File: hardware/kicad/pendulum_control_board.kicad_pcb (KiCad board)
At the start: 2 copper layers, 103.3 x 112.3 mm, 267 parts, among them IC1 STM32F411CEU6, IC2 LM358D, J1 DX07S024JJ2, Q1 BSS138, Q2 BSS138, Q3 BSS138, Q4 BSS138, Q5 2N7002, Q6 2N7002, Q7 2N7002, U1 FT231XS, U2 V_REG_317SMD, U3 V_REG_317SMD, U5 LTC6102DD, X1 5566-8, X2 5566-8, Y2 32.768kHz

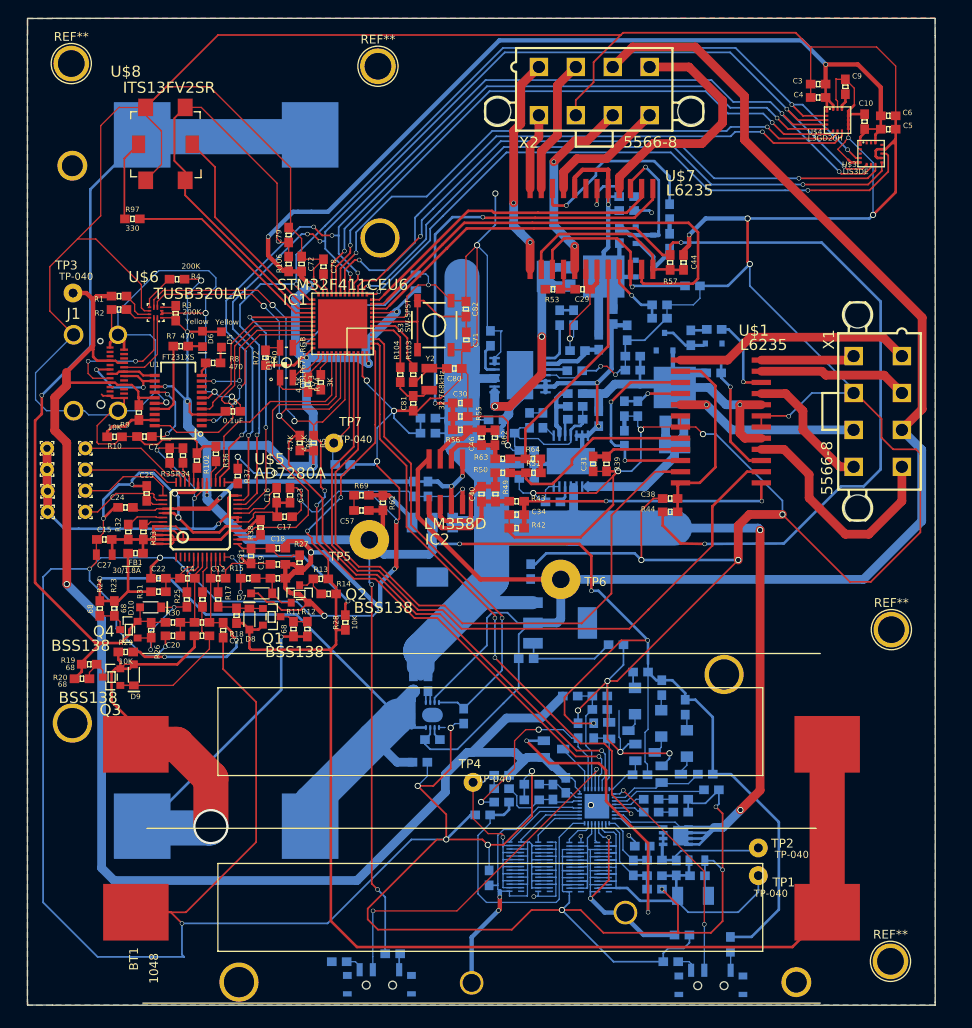
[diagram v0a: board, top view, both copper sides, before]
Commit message: updated PCB and created schematic pdf
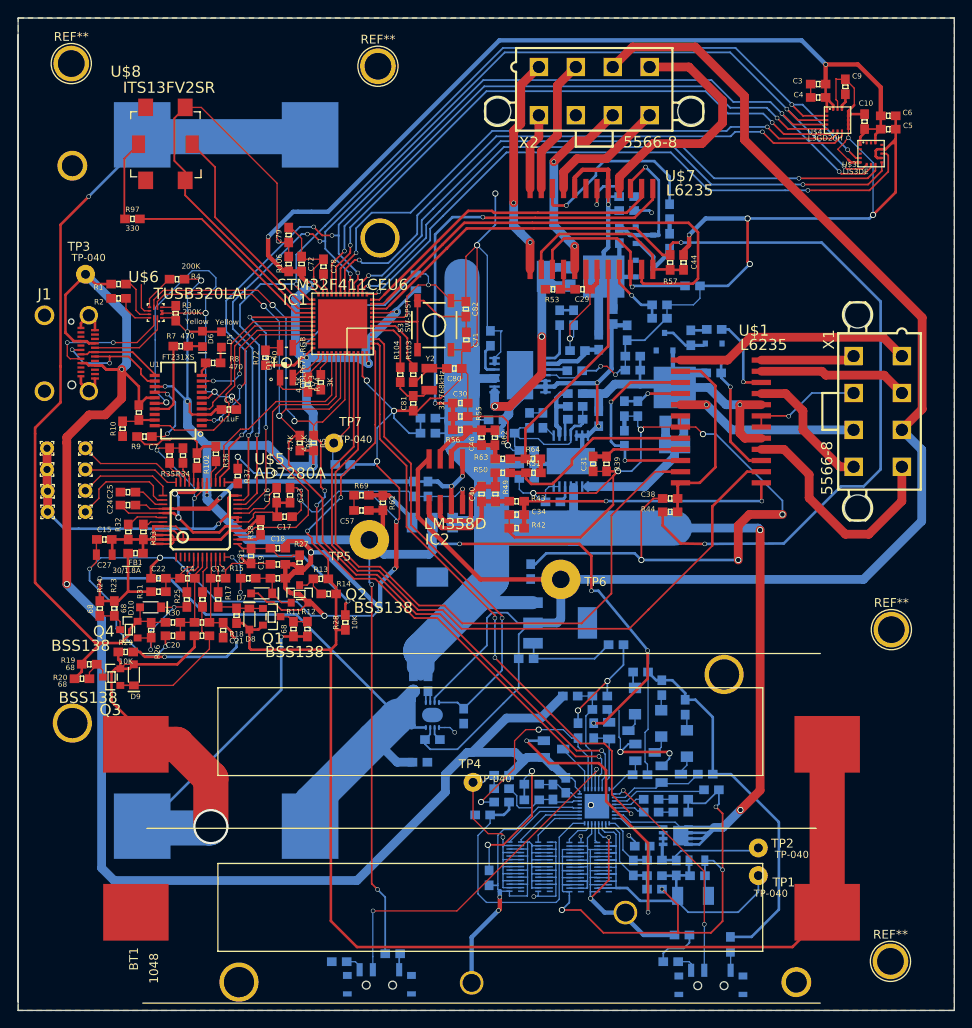
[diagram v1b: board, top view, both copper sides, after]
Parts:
- moved J1 3.99 mm to (53.6, 84.6)
- moved TP3 2.56 mm to (55.3, 79.2)
- moved C25 2.14 mm to (60.1, 104.0), turned to 180 degrees
- moved R1 1.37 mm to (59.0, 80.3)
- moved R10 1.29 mm to (59.5, 96.8), turned to 90 degrees
- moved R2 1.27 mm to (59.0, 81.9)
- moved C8 0.50 mm to (71.6, 94.6)
- moved C24 0.39 mm to (60.1, 105.5)
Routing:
- net GND: track 1439.6 -> 869.8 mm, vias 64 -> 59
- net /3P3V: track 422.8 -> 415.6 mm
- net /DP: track 5.36 -> 9.68 mm
- net /V_BUS: track 194.3 -> 190.8 mm, vias 1 -> 2
- net /N$10: track 6.55 -> 3.72 mm
- net /DM: track 12.3 -> 15.0 mm
- net /T_CELL1: track 10.3 -> 12.4 mm
- net /CREF: track 1.69 -> 3.71 mm
- net /UART_RXD: track 29.4 -> 27.6 mm
- net /N$6: track 3.91 -> 5.49 mm
- net /N$1: track 3.01 -> 4.31 mm
- net /DEN_GYRO: track 69.9 -> 68.8 mm
- net /CC2: track 15.8 -> 14.8 mm
- net /CC1: track 8.58 -> 9.30 mm
- net /ALERT_BATT: track 24.6 -> 23.9 mm
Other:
- board size 103.3 x 112.3 mm -> 106.5 x 112.9 mm

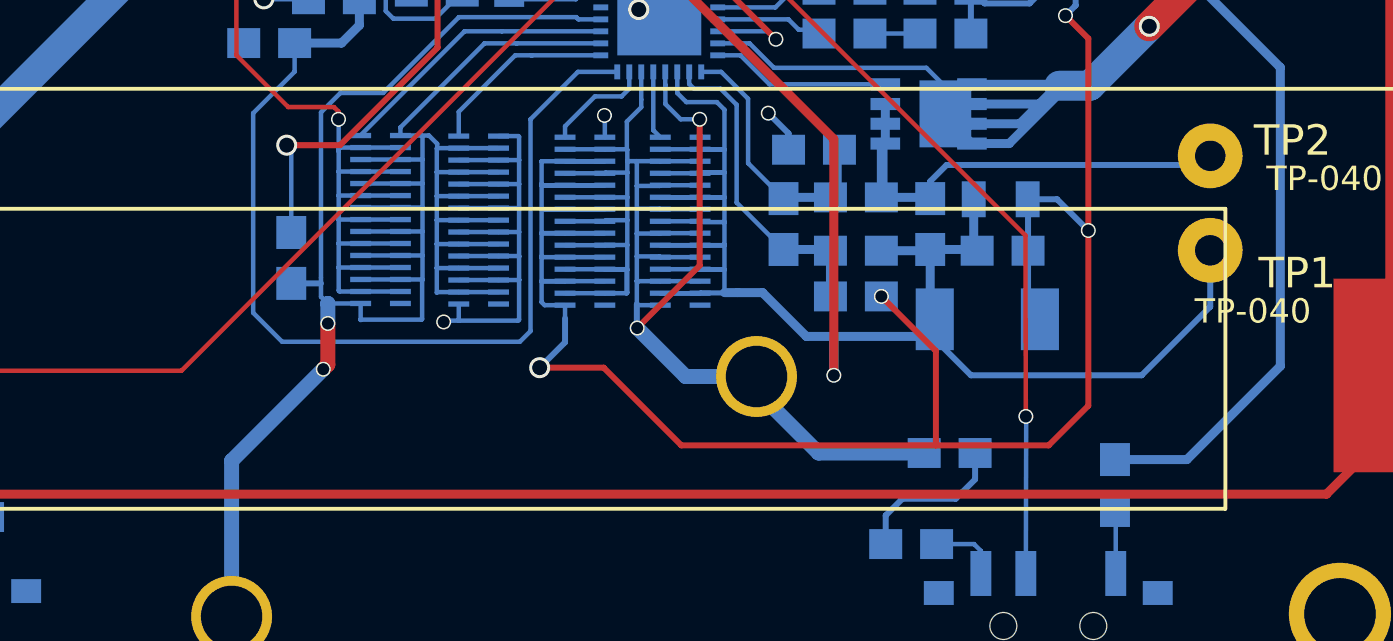
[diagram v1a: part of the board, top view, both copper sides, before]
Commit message: added schottkys to charging circuit
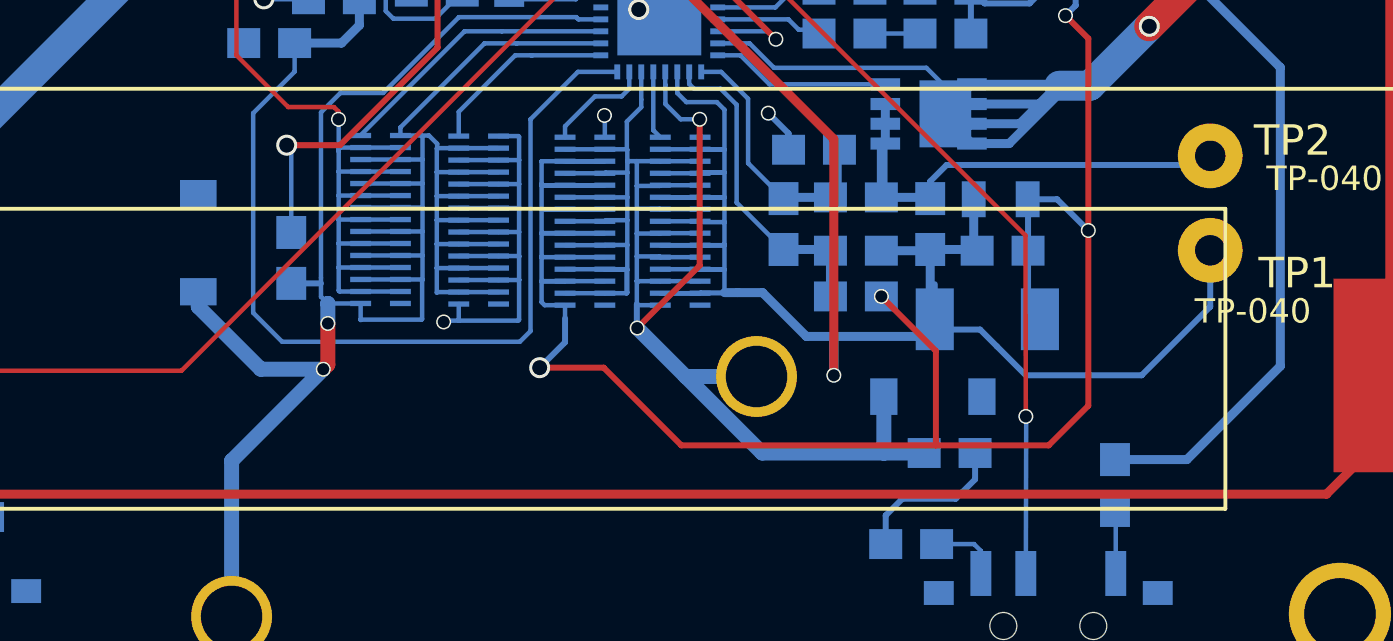
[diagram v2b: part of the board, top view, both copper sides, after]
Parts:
- added D1: MBR0520, Diodes_SMD:SOD-123, B.Cu at (98.1, 147.4)
- added D17: MBR0520, Diodes_SMD:SOD-123, B.Cu at (122.6, 152.5)
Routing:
- net /N$62: track 81.0 -> 86.5 mm
- net /N$65: track 65.6 -> 70.1 mm
- net /VSYS+: track 93.7 -> 94.5 mm
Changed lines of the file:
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@@
 (kicad_pcb (version 4) (host pcbnew 4.0.2+dfsg1-stable)
   (general
-    (links 731)
+    (links 735)
     (no_connects 0)
-    (area 44.840853 50.026099 152.005501 163.209581)
+    (area 47.536899 49.987999 154.177201 163.016401)
     (thickness 1.6)
     (drawings 6)
-    (tracks 2909)
+    (tracks 2920)
     (zones 0)
-    (modules 267)
+    (modules 269)
     (nets 195)
   )
@@
   )
   (setup
-    (last_trace_width 0.2)
+    (last_trace_width 0.5)
     (user_trace_width 0.15)
     (user_trace_width 0.2)
@@
     (pad 1 thru_hole circle (at 0 0) (size 4.064 4.064) (drill 3.048) (layers *.Cu *.Mask F.SilkS))
   )
+  (module Diodes_SMD:SOD-123 (layer B.Cu)
+    (at 98.0948 147.3708 90)
+    (descr SOD-123)
+    (tags SOD-123)
+    (attr smd)
+    (fp_text reference D1 (at 2.8956 -0.254 180) (layer B.SilkS)
+      (effects (font (size 1 1) (thickness 0.15)) (justify mirror))
+    )
+    (fp_text value MBR0520 (at 0.6604 -1.8796 90) (layer B.SilkS)
+      (effects (font (size 1 1) (thickness 0.15)) (justify mirror))
+    )
+    (fp_line (start 0.3175 0) (end 0.6985 0) (layer B.SilkS) (width 0.15))
+    (fp_line (start -0.6985 0) (end -0.3175 0) (layer B.SilkS) (width 0.15))
+    (fp_line (start -0.3175 0) (end 0.3175 0.381) (layer B.SilkS) (width 0.15))
+    (fp_line (start 0.3175 0.381) (end 0.3175 -0.381) (layer B.SilkS) (width 0.15))
+    (fp_line (start 0.3175 -0.381) (end -0.3175 0) (layer B.SilkS) (width 0.15))
+    (fp_line (start -0.3175 0.508) (end -0.3175 -0.508) (layer B.SilkS) (width 0.15))
+    (fp_line (start -2.25 1.05) (end 2.25 1.05) (layer B.CrtYd) (width 0.05))
+    (fp_line (start 2.25 1.05) (end 2.25 -1.05) (layer B.CrtYd) (width 0.05))
+    (fp_line (start 2.25 -1.05) (end -2.25 -1.05) (layer B.CrtYd) (width 0.05))
+    (fp_line (start -2.25 1.05) (end -2.25 -1.05) (layer B.CrtYd) (width 0.05))
+    (fp_line (start -2 -0.9) (end 1.54 -0.9) (layer B.SilkS) (width 0.15))
+    (fp_line (start -2 0.9) (end 1.54 0.9) (layer B.SilkS) (width 0.15))
+    (pad 1 smd rect (at -1.635 0 90) (size 0.91 1.22) (layers B.Cu B.Paste B.Mask)
+      (net 47 /N$62))
+    (pad 2 smd rect (at 1.635 0 90) (size 0.91 1.22) (layers B.Cu B.Paste B.Mask)
+      (net 1 GND))
+  )
+  (module Diodes_SMD:SOD-123 (layer B.Cu)
+    (at 122.5804 152.5016)
+    (descr SOD-123)
+    (tags SOD-123)
+    (attr smd)
+    (fp_text reference D17 (at 3.7592 0.6096) (layer B.SilkS)
+      (effects (font (size 1 1) (thickness 0.15)) (justify mirror))
+    )
+    (fp_text value MBR0520 (at -3.6576 3.2004 90) (layer B.SilkS)
+      (effects (font (size 1 1) (thickness 0.15)) (justify mirror))
+    )
+    (fp_line (start 0.3175 0) (end 0.6985 0) (layer B.SilkS) (width 0.15))
+    (fp_line (start -0.6985 0) (end -0.3175 0) (layer B.SilkS) (width 0.15))
+    (fp_line (start -0.3175 0) (end 0.3175 0.381) (layer B.SilkS) (width 0.15))
+    (fp_line (start 0.3175 0.381) (end 0.3175 -0.381) (layer B.SilkS) (width 0.15))
+    (fp_line (start 0.3175 -0.381) (end -0.3175 0) (layer B.SilkS) (width 0.15))
+    (fp_line (start -0.3175 0.508) (end -0.3175 -0.508) (layer B.SilkS) (width 0.15))
+    (fp_line (start -2.25 1.05) (end 2.25 1.05) (layer B.CrtYd) (width 0.05))
+    (fp_line (start 2.25 1.05) (end 2.25 -1.05) (layer B.CrtYd) (width 0.05))
+    (fp_line (start 2.25 -1.05) (end -2.25 -1.05) (layer B.CrtYd) (width 0.05))
+    (fp_line (start -2.25 1.05) (end -2.25 -1.05) (layer B.CrtYd) (width 0.05))
+    (fp_line (start -2 -0.9) (end 1.54 -0.9) (layer B.SilkS) (width 0.15))
+    (fp_line (start -2 0.9) (end 1.54 0.9) (layer B.SilkS) (width 0.15))
+    (pad 1 smd rect (at -1.635 0) (size 0.91 1.22) (layers B.Cu B.Paste B.Mask)
+      (net 48 /N$65))
+    (pad 2 smd rect (at 1.635 0) (size 0.91 1.22) (layers B.Cu B.Paste B.Mask)
+      (net 1 GND))
+  )
   (gr_line (start 47.5996 50.038) (end 47.5996 50.0888) (angle 90) (layer Edge.Cuts) (width 0.1))
   (gr_line (start 154.1272 50.038) (end 47.5996 50.038) (angle 90) (layer Edge.Cuts) (width 0.1))
@@
   (segment (start 112.2045 132.842) (end 112.2045 129.45364) (width 0.15) (layer B.Cu) (net 46))
   (segment (start 112.85982 133.49732) (end 112.2045 132.842) (width 0.15) (layer B.Cu) (net 46))
+  (segment (start 98.0948 149.0058) (end 98.0948 149.5044) (width 0.5) (layer B.Cu) (net 47) (status 400000))
+  (segment (start 100.1776 151.5872) (end 102.2604 151.5872) (width 0.5) (layer B.Cu) (net 47))
+  (segment (start 98.0948 149.5044) (end 100.1776 151.5872) (width 0.5) (layer B.Cu) (net 47))
   (segment (start 99.20478 159.82696) (end 99.20478 154.64282) (width 0.5) (layer B.Cu) (net 47))
   (segment (start 102.4128 149.39645) (end 102.40645 149.39645) (width 0.5) (layer B.Cu) (net 47))
@@
   (segment (start 106.05516 144.21866) (end 106.045 144.22882) (width 0.15) (layer B.Cu) (net 47))
   (segment (start 106.045 144.22882) (end 106.045 145.01876) (width 0.15) (layer B.Cu) (net 47))
+  (segment (start 120.9454 152.5016) (end 120.9454 154.3812) (width 0.5) (layer B.Cu) (net 48) (status 400000))
+  (segment (start 120.9548 154.3304) (end 120.9548 154.3812) (width 0.5) (layer B.Cu) (net 48))
+  (segment (start 120.9548 154.3718) (end 120.9548 154.3304) (width 0.5) (layer B.Cu) (net 48))
+  (segment (start 120.9454 154.3812) (end 120.9548 154.3718) (width 0.5) (layer B.Cu) (net 48))
+  (segment (start 122.29084 154.3812) (end 120.9548 154.3812) (width 0.5) (layer B.Cu) (net 48) (status 400000))
+  (segment (start 120.9548 154.3812) (end 116.8908 154.3812) (width 0.5) (layer B.Cu) (net 48))
+  (segment (start 116.8908 154.3812) (end 114.34064 151.83104) (width 0.5) (layer B.Cu) (net 48))
   (segment (start 110.31982 144.25676) (end 111.6457 144.25676) (width 0.15) (layer B.Cu) (net 48))
   (segment (start 111.6457 144.25676) (end 112.37976 144.25676) (width 0.15) (layer B.Cu) (net 48))
@@
   (segment (start 114.34064 151.83104) (end 112.7252 150.2156) (width 0.5) (layer B.Cu) (net 48))
   (segment (start 116.70284 151.83104) (end 116.70284 152.31364) (width 0.5) (layer B.Cu) (net 48))
-  (segment (start 116.70284 152.31364) (end 118.7704 154.3812) (width 0.5) (layer B.Cu) (net 48))
-  (segment (start 118.7704 154.3812) (end 122.29084 154.3812) (width 0.5) (layer B.Cu) (net 48))
   (segment (start 114.808 143.256) (end 114.808 148.1328) (width 0.2) (layer F.Cu) (net 48))
   (segment (start 114.808 148.1328) (end 112.7252 150.2156) (width 0.2) (layer F.Cu) (net 48))
@@
   (segment (start 94.99092 130.7719) (end 94.99092 131.54406) (width 0.2) (layer B.Cu) (net 55))
   (segment (start 94.99092 131.54406) (end 95.59036 132.1435) (width 0.2) (layer B.Cu) (net 55))
+  (segment (start 125.6792 151.7904) (end 124.714 150.8252) (width 0.2) (layer B.Cu) (net 56))
+  (segment (start 125.6792 151.7904) (end 129.54 151.7904) (width 0.2) (layer B.Cu) (net 56))
+  (segment (start 129.54 151.7904) (end 131.826 149.5044) (width 0.2) (layer B.Cu) (net 56))
+  (segment (start 131.826 147.6248) (end 131.826 149.5044) (width 0.2) (layer B.Cu) (net 56))
+  (segment (start 124.1552 150.2664) (end 122.9868 150.2664) (width 0.2) (layer B.Cu) (net 56) (status 800000))
+  (segment (start 124.714 150.8252) (end 124.1552 150.2664) (width 0.2) (layer B.Cu) (net 56))
+  (segment (start 122.9868 150.2664) (end 122.6439 149.9235) (width 0.2) (layer B.Cu) (net 56) (status C00000))
   (segment (start 114.06124 141.67612) (end 114.06124 142.38224) (width 0.15) (layer B.Cu) (net 56))
   (segment (start 113.49482 145.05686) (end 114.8207 145.05686) (width 0.15) (layer B.Cu) (net 56))
@@
   (segment (start 113.49482 147.45462) (end 114.8207 147.45462) (width 0.15) (layer B.Cu) (net 56))
   (segment (start 114.8207 147.45462) (end 115.6335 147.45462) (width 0.15) (layer B.Cu) (net 56))
-  (segment (start 122.6439 149.9235) (end 122.6439 150.5839) (width 0.2) (layer B.Cu) (net 56))
-  (segment (start 122.6439 150.5839) (end 123.8504 151.7904) (width 0.2) (layer B.Cu) (net 56))
-  (segment (start 131.826 149.5044) (end 131.826 147.6248) (width 0.2) (layer B.Cu) (net 56))
-  (segment (start 129.54 151.7904) (end 131.826 149.5044) (width 0.2) (layer B.Cu) (net 56))
-  (segment (start 123.8504 151.7904) (end 129.54 151.7904) (width 0.2) (layer B.Cu) (net 56))
+  (segment (start 122.6439 149.9235) (end 122.6439 148.7551) (width 0.2) (layer B.Cu) (net 56))
   (segment (start 107.42168 132.27558) (end 105.46842 132.27558) (width 0.3) (layer B.Cu) (net 56))
   (segment (start 119.2784 151.7904) (end 119.2784 150.495) (width 0.3) (layer B.Cu) (net 56))

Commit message: added bom and updated board
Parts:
- C36, C39, C42, C45: footprint SPARKFUN-CAPACITORS_0603 -> Capacitors_SMD:C_1206
- D11, D12, D13, D14: footprint ADAFRUIT_SOT23-R -> Diodes_SMD:SOD-123
- R105: value (none) -> 100K
- R43, R56: value (none) -> 5.6K
- R47, R65: value 185K -> 187K
- R49, R62: value (none) -> 1M
- R50, R63: value (none) -> 4.7K
- R51, R64: value (none) -> 1K
- R75: value (none) -> 4.7
- R78: value (none) -> 402K
- R79: value (none) -> 107K
- R81, R82, R86, R87: value (none) -> 1
- R83: value (none) -> 0
- R84: value (none) -> 2K
- R85: value (none) -> 115K
- R88: value (none) -> 0.01
- R99: footprint SPARKFUN-RESISTORS_0603 -> Resistors_SMD:R_1206
- moved C43 11.4 mm to (124.4, 78.9)
- moved C36 10.0 mm to (127.6, 90.3), turned to 180 degrees
- moved C35 8.66 mm to (135.1, 88.0)
- moved R41 7.75 mm to (131.7, 88.0), turned to 180 degrees
- moved D11 6.54 mm to (127.6, 85.8), turned to 0 degrees
- moved C39 4.95 mm to (122.4, 88.1)
- moved C42 4.52 mm to (113.0, 74.4), turned to 270 degrees
- moved D13 4.24 mm to (117.9, 74.4), turned to 270 degrees
- moved D14 3.22 mm to (119.3, 77.9), turned to 180 degrees
- moved R99 2.49 mm to (90.2, 125.0)
- moved R54 1.98 mm to (119.8, 75.1)
- moved C32 1.96 mm to (119.8, 71.8)
- moved C37 1.73 mm to (117.9, 90.2)
- moved C28 1.04 mm to (120.1, 81.7)
- moved R52 1.04 mm to (120.1, 83.3)
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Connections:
- D11 pad 1: /V_DRIVER_X -> /N$47
- D11 pad 2: (no net) -> Net-(D11-Pad2)
- D12 pad 1: /N$48 -> Net-(D11-Pad2)
- D12 pad 2: (no net) -> /V_DRIVER_X
- D13 pad 1: /V_DRIVER_Y -> /N$45
- D13 pad 2: (no net) -> Net-(D13-Pad2)
- D14 pad 1: /N$46 -> Net-(D13-Pad2)
- D14 pad 2: (no net) -> /V_DRIVER_Y
- R41 pad 2: /N$48 -> Net-(D11-Pad2)
- R54 pad 2: /N$46 -> Net-(D13-Pad2)
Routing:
- net /N$45: track 21.2 -> 7.24 mm
- net /N$52: track 21.7 -> 14.0 mm
- net /N$47: track 14.7 -> 22.4 mm
- net /N$46: track 7.01 -> 0.00 mm
- net /V_DRIVER_Y: track 41.7 -> 48.5 mm
- net /N$48: track 6.78 -> 0.00 mm
- net /V_CELL4: track 94.8 -> 89.5 mm
- net Net-(D13-Pad2): track 0.00 -> 4.42 mm
- net /V_DRIVER_X: track 44.3 -> 48.5 mm
- net Net-(D11-Pad2): track 0.00 -> 3.87 mm
- net GND: track 869.8 -> 866.0 mm
- net /N$50: track 9.54 -> 7.15 mm
- net /V_BATT: track 220.4 -> 221.7 mm
- net /N$35: track 7.83 -> 7.00 mm
